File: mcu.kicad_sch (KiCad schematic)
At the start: 27 parts, among them J6 Conn_01x08, J7 Conn_01x02, U5 AT25XE321D-UUN-T, U6 EFM32PG23B200F512IM40, Y2 39MHz

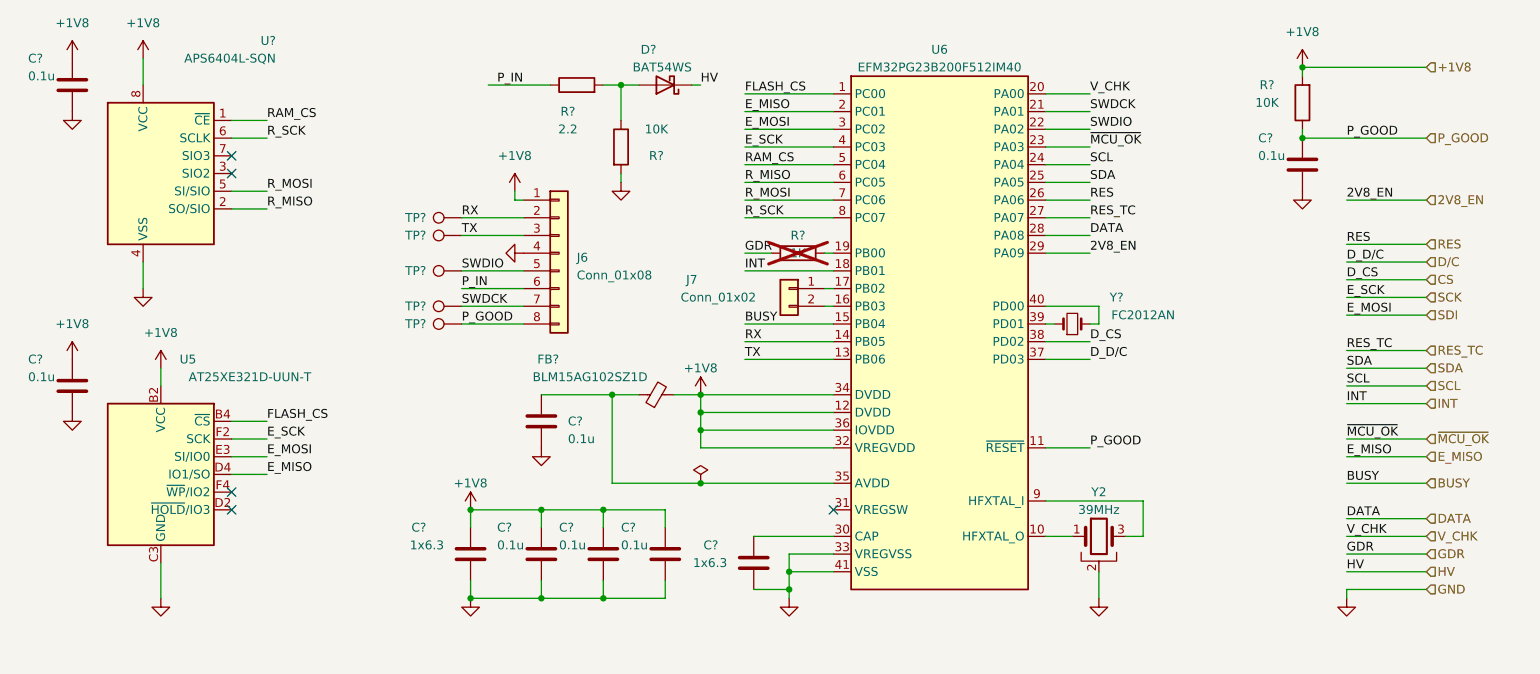
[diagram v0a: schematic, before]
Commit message: Fix capacitor values
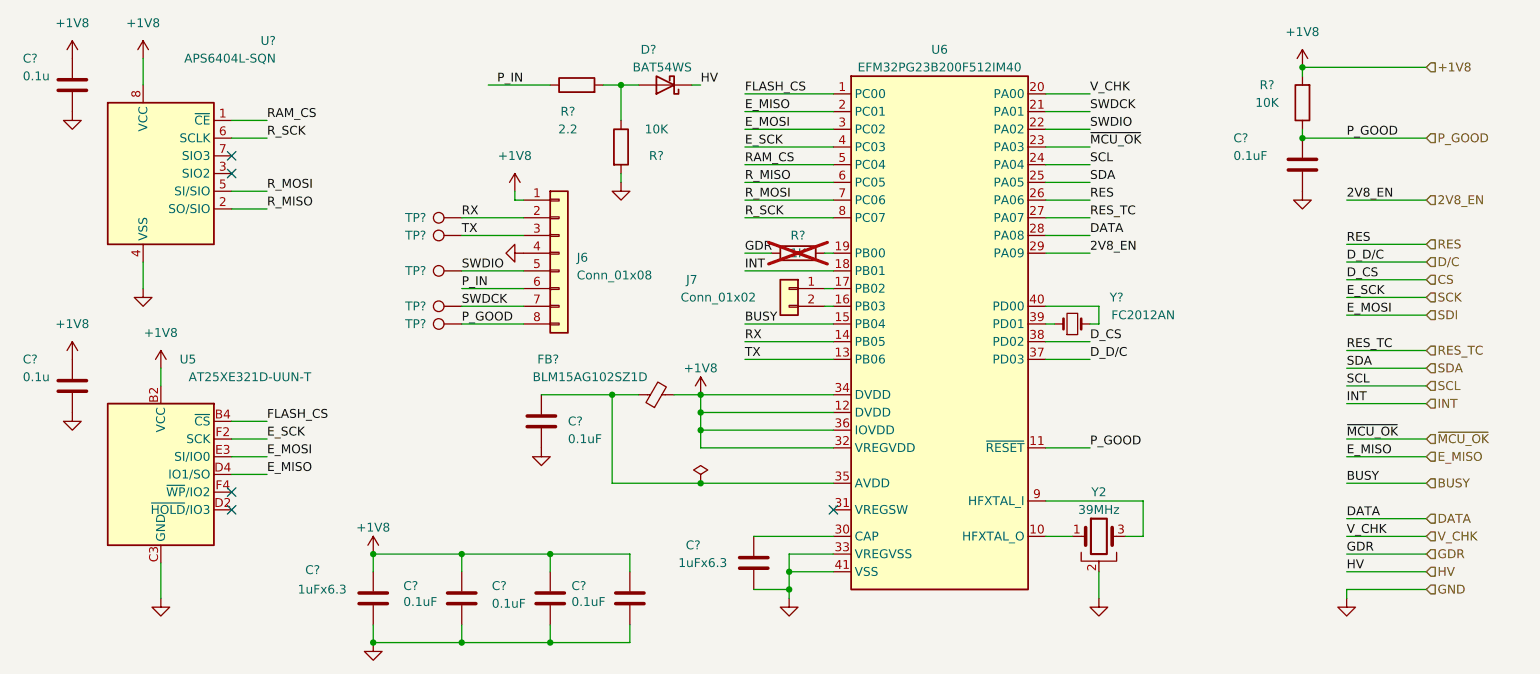
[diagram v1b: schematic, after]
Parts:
- C? (x5): value 0.1u -> 0.1uF
- C? (x2): value 1x6.3 -> 1uFx6.3
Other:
- moved on the sheet: C?

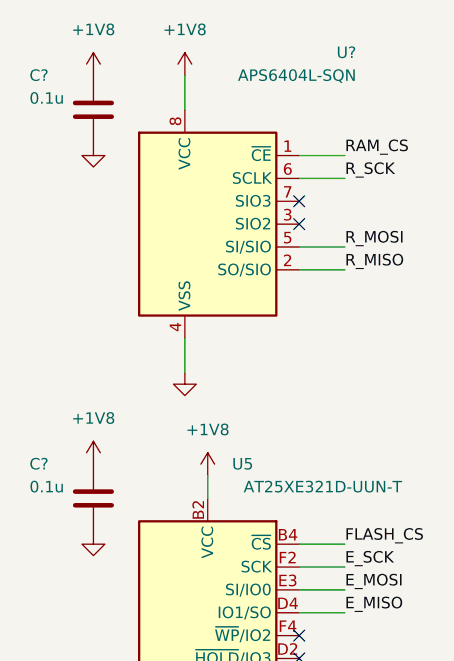
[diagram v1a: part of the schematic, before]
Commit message: Fill up mouser part numbers
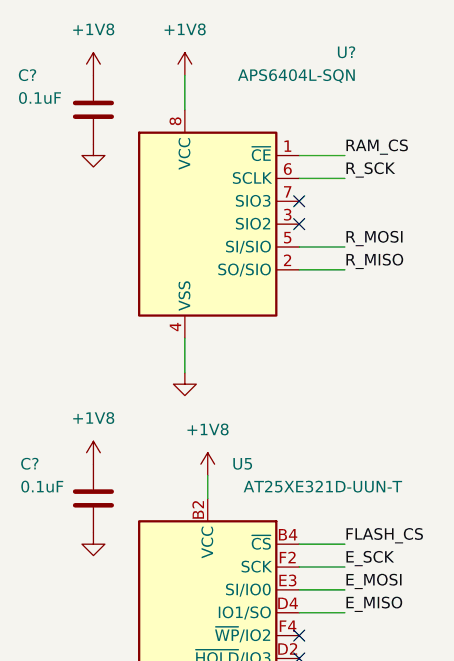
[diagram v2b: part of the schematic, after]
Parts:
- C? (x5): MouserPN (none) -> 581-KGM05AR71C104KN
- C? (x2): value 0.1u -> 0.1uF; MouserPN (none) -> 581-KGM05AR71C104KN
- C? (x2): MouserPN (none) -> 963-JMK105BJ105KV-F
- D?: MouserPN (none) -> 621-BAT54WS-F
- FB?: MouserPN (none) -> 81-BLM15AG102SZ1D
- R?: now left out of the parts list
- U5: MouserPN (none) -> 988-AT25XE321D-UUN-T
- U6: MouserPN (none) -> 634-PG23200F512IM40C
- U?: MouserPN (none) -> 878-APS6404L-SQN-SN
- Y2: MouserPN (none) -> 520-ECS-390-CDX-2289
- Y?: MouserPN (none) -> 732-F32768K90NN60KC7

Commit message: Finish BOM components filling
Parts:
- J6, J7, TP? (x5): now left out of the parts list
- R?: MouserPN (none) -> 71-CRCW06032R20FNEA
- R? (x2): MouserPN (none) -> 71-CRCW040210K0FKEDC
- R?: MouserPN (none) -> 603-RC0402FR-071KL
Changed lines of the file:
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@@
 			)
 		)
-		(property "MouserPN" ""
+		(property "MouserPN" "71-CRCW06032R20FNEA"
 			(at 119.38 53.34 0)
 			(effects
@@
 		(unit 1)
 		(exclude_from_sim no)
-		(in_bom yes)
+		(in_bom no)
 		(on_board yes)
 		(dnp no)
@@
 			)
 		)
-		(property "MouserPN" ""
+		(property "MouserPN" "71-CRCW040210K0FKEDC"
 			(at 223.52 55.88 0)
 			(effects
@@
 			)
 		)
-		(property "MouserPN" ""
+		(property "MouserPN" "603-RC0402FR-071KL"
 			(at 151.13 77.47 0)
 			(effects
@@
 		(unit 1)
 		(exclude_from_sim no)
-		(in_bom yes)
+		(in_bom no)
 		(on_board yes)
 		(dnp no)
@@
 			)
 		)
-		(property "MouserPN" ""
+		(property "MouserPN" "71-CRCW040210K0FKEDC"
 			(at 125.73 62.23 0)
 			(effects
@@
 		(unit 1)
 		(exclude_from_sim no)
-		(in_bom yes)
+		(in_bom no)
 		(on_board yes)
 		(dnp no)
@@
 		(unit 1)
 		(exclude_from_sim no)
-		(in_bom yes)
+		(in_bom no)
 		(on_board yes)
 		(dnp no)
@@
 		(unit 1)
 		(exclude_from_sim no)
-		(in_bom yes)
+		(in_bom no)
 		(on_board yes)
 		(dnp no)
@@
 		(unit 1)
 		(exclude_from_sim no)
-		(in_bom yes)
+		(in_bom no)
 		(on_board yes)
 		(dnp no)
@@
 		(unit 1)
 		(exclude_from_sim no)
-		(in_bom yes)
+		(in_bom no)
 		(on_board yes)
 		(dnp no)
